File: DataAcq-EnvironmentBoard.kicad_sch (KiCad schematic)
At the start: 23 parts, among them J1 CAN Output, J2 CAN Input, U1 SHT45, U2 FS3000-1005, U3 LMT87DCK, U4 Daughterboard Connector

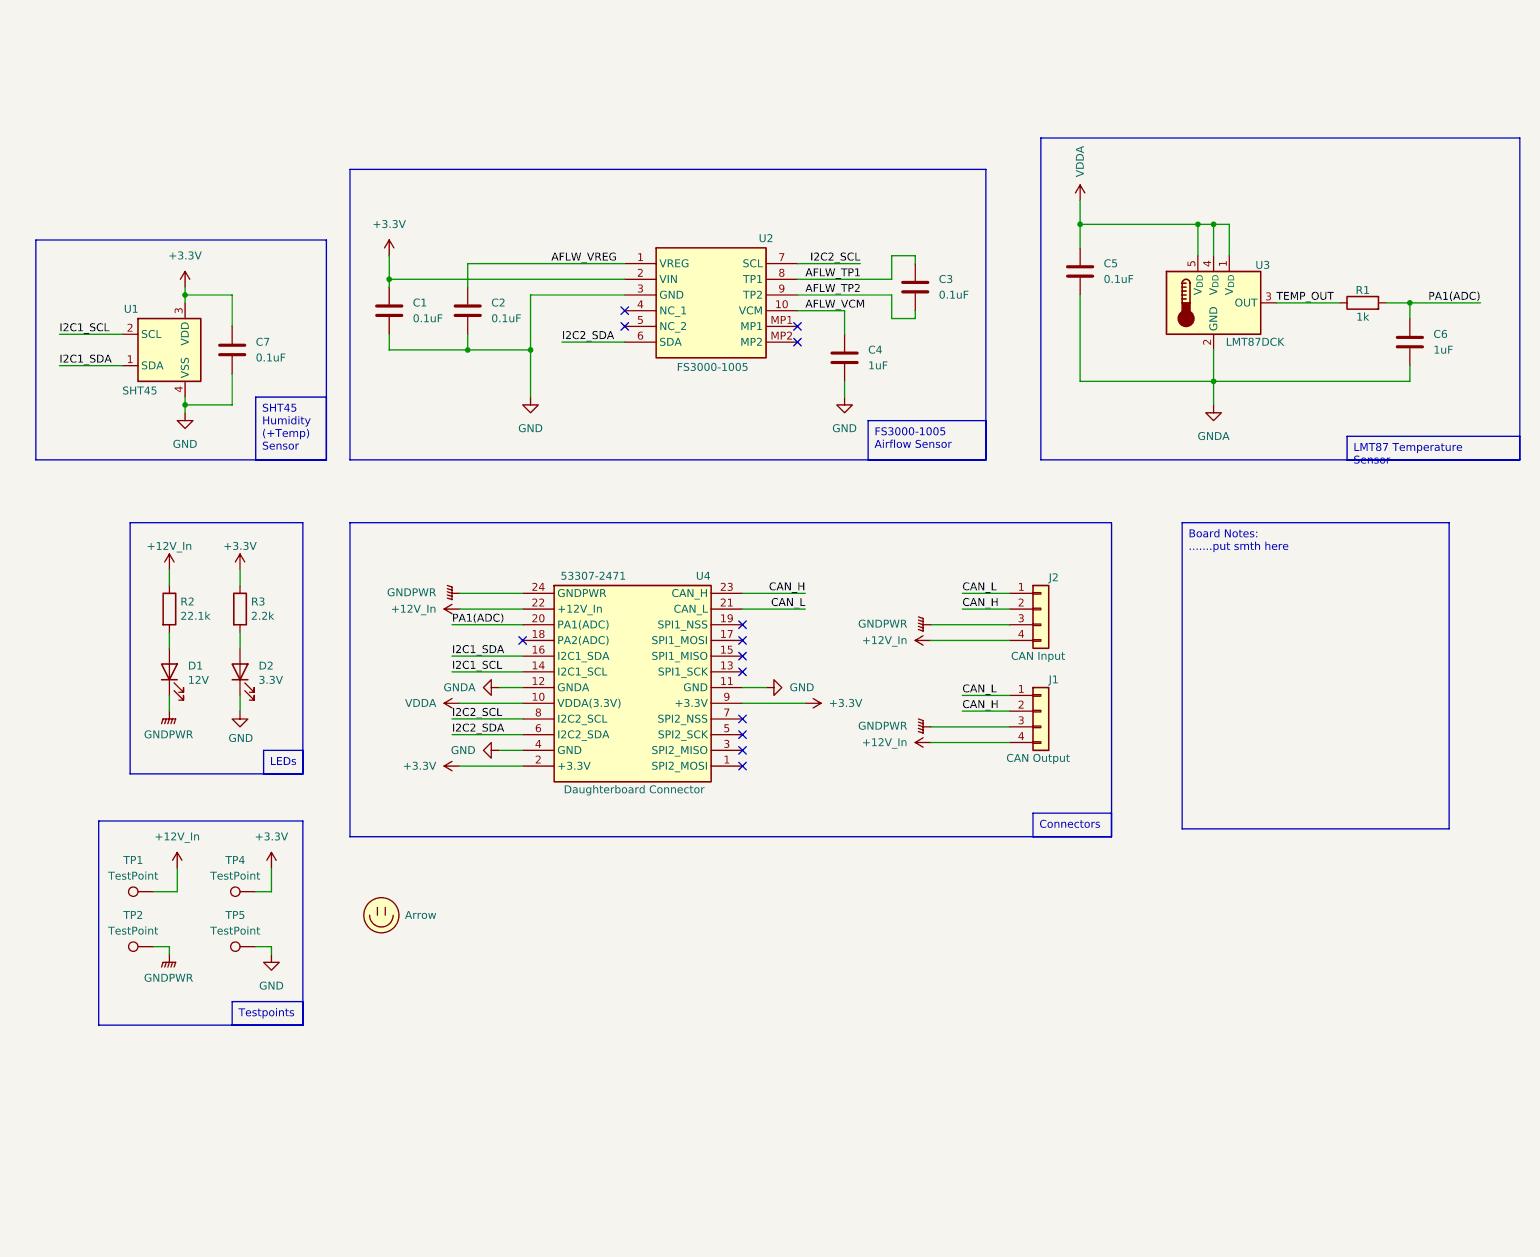
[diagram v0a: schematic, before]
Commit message: change sch to match new symbols
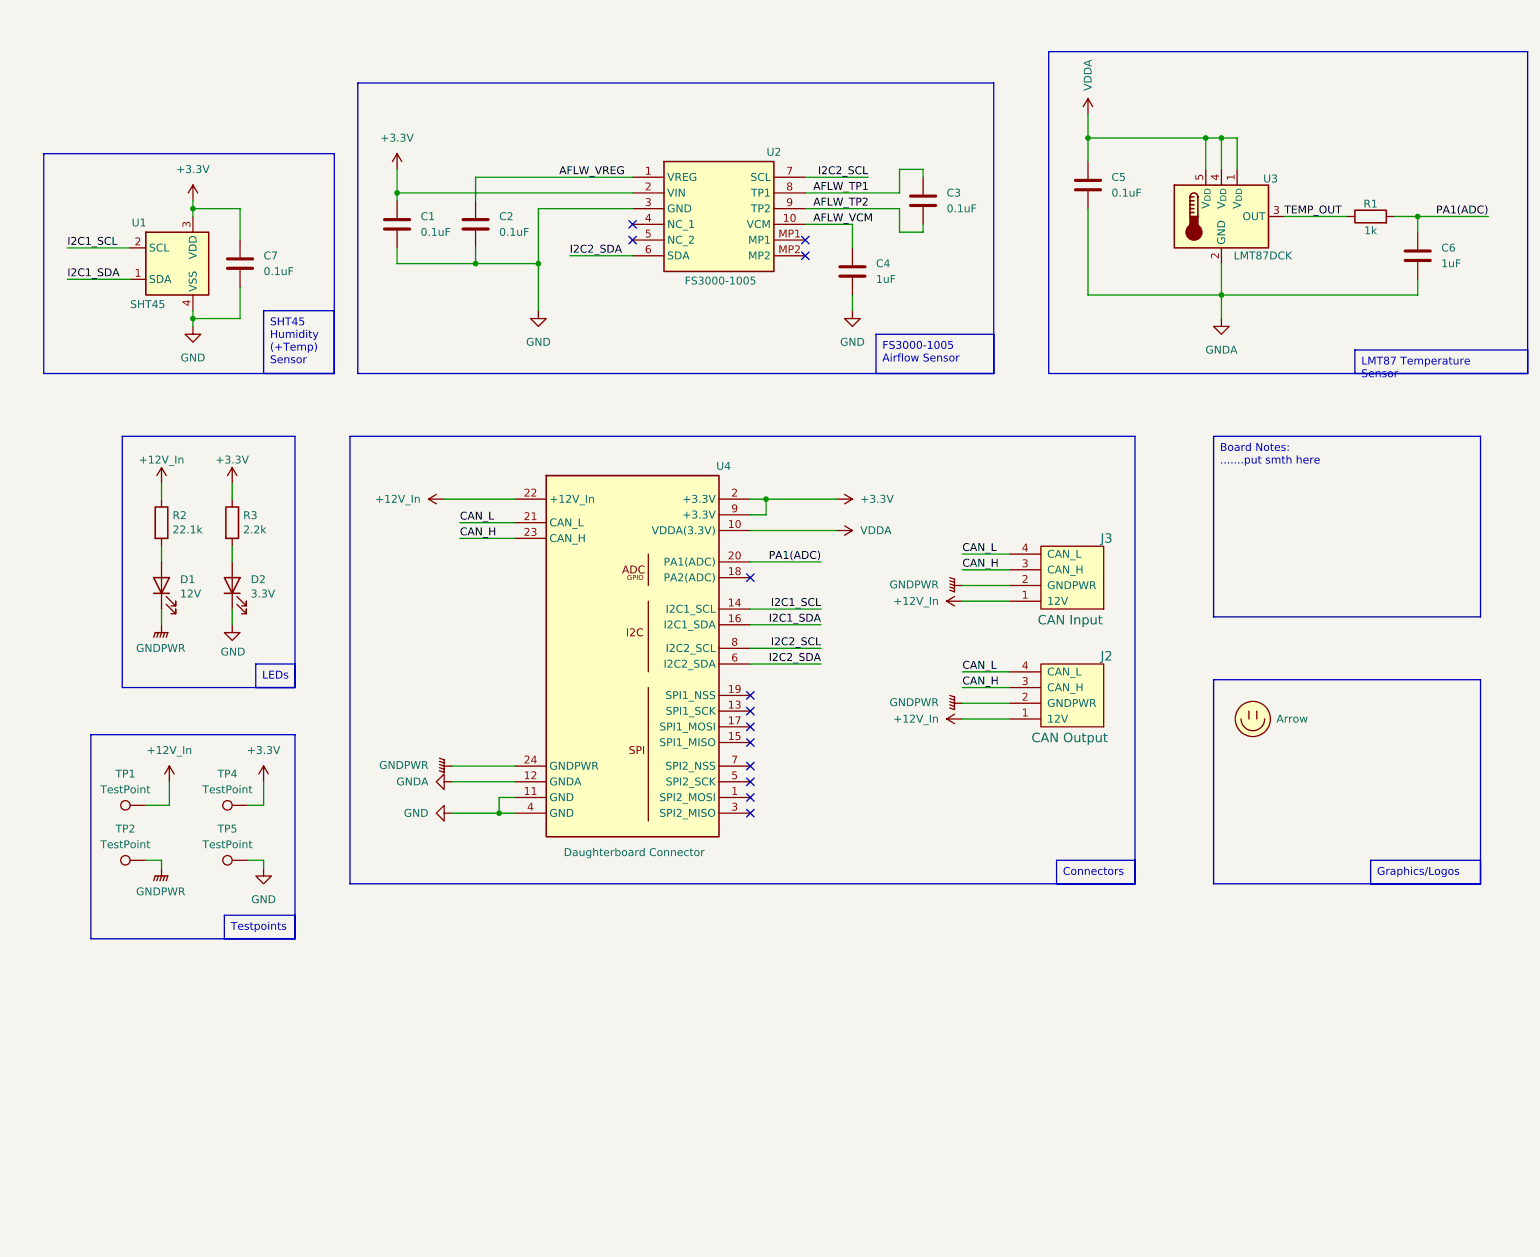
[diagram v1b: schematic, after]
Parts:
- removed J1: CAN Output, UTSVT_Connectors:Molex_MicroFit3.0_1x4xP3.00mm_PolarizingPeg_Vertical, symbol Connector_Generic:Conn_01x04
- removed J2: CAN Input, UTSVT_Connectors:Molex_MicroFit3.0_1x4xP3.00mm_PolarizingPeg_Vertical, symbol Connector_Generic:Conn_01x04
- added J2: CAN Output, UTSVT_Connectors:Molex_MicroFit3.0_1x4xP3.00mm_PolarizingPeg_Vertical, symbol utsvt-connectors:PeripheralCANConnector
- added J3: CAN Input, UTSVT_Connectors:Molex_MicroFit3.0_1x4xP3.00mm_PolarizingPeg_Vertical, symbol utsvt-connectors:PeripheralCANConnector
- U2: footprint SamacSys_Parts:FS30001005 -> FS30001005
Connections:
- net +12V_In: now also J2.1 (12V), J3.1 (12V)
- net CAN_H: now also J2.3 (CAN_H), J3.3 (CAN_H)
- net CAN_L: now also J2.4 (CAN_L), J3.4 (CAN_L)
- net GNDPWR: now also J2.2 (GNDPWR), J3.2 (GNDPWR)
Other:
- moved on the sheet: C1, C2, C3, C4, C5, C6, C7, D1, D2, R1, R2, R3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

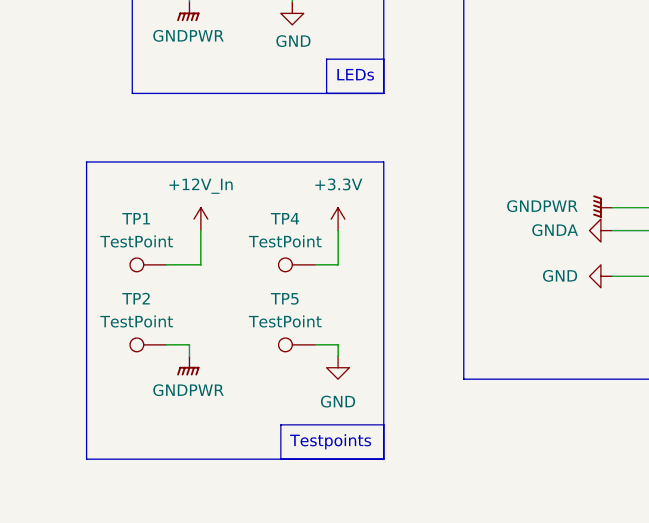
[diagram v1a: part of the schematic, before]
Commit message: add test point and redo CAN connections
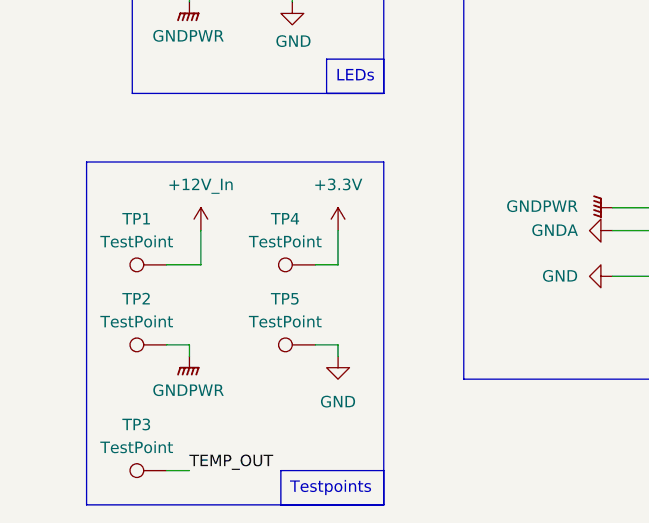
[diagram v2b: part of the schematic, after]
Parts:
- added TP3: TestPoint, UTSVT_Special:TestPoint_HEX_3mmID, symbol Connector:TestPoint
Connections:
- net TEMP_OUT: now also TP3.1
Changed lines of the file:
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@@
 	(wire
 		(pts
+			(xy 45.72 166.37) (xy 48.26 166.37)
+		)
+		(stroke
+			(width 0)
+			(type default)
+		)
+	)
+	(wire
+		(pts
 			(xy 160.02 60.96) (xy 160.02 63.5)
 		)
@@
 	(rectangle
 		(start 36.83 132.08)
-		(end 69.85 165.1)
+		(end 69.85 170.18)
 		(stroke
 			(width 0)
@@
 	(text_box "Testpoints"
 		(exclude_from_sim no)
-		(at 58.42 161.29 0)
+		(at 58.42 166.37 0)
 		(size 11.43 3.81)
 		(stroke
@@
 		)
 	)
+	(label "TEMP_OUT"
+		(at 48.26 166.37 0)
+		(fields_autoplaced yes)
+		(effects
+			(font
+				(size 1.27 1.27)
+			)
+			(justify left bottom)
+		)
+	)
 	(symbol
 		(lib_id "utsvt-connectors:PeripheralCANConnector")
@@
 					(unit 1)
 				)
+			)
+		)
+	)
+	(symbol
+		(lib_id "Connector:TestPoint")
+		(at 45.72 166.37 90)
+		(unit 1)
+		(exclude_from_sim no)
+		(in_bom yes)
+		(on_board yes)
+		(dnp no)
+		(fields_autoplaced yes)
+		(property "Reference" "TP3"
+			(at 42.418 161.29 90)
+			(effects
+				(font
+					(size 1.27 1.27)
+				)
+			)
+		)
+		(property "Value" "TestPoint"
+			(at 42.418 163.83 90)
+			(effects
+				(font
+					(size 1.27 1.27)
+				)
+			)
+		)
+		(property "Footprint" "UTSVT_Special:TestPoint_HEX_3mmID"
+			(at 45.72 161.29 0)
+			(effects
+				(font
+					(size 1.27 1.27)
+				)
+				(hide yes)
+			)
+		)
+		(property "Datasheet" "~"
+			(at 45.72 161.29 0)
+			(effects
+				(font
+					(size 1.27 1.27)
+				)
+				(hide yes)
+			)
+		)
+		(property "Description" "test point"
+			(at 45.72 166.37 0)
+			(effects
+				(font
+					(size 1.27 1.27)
+				)
+				(hide yes)
+			)
+		)
+		(property "PN" ""
+			(at 45.72 166.37 0)
+			(effects
+				(font
+					(size 1.27 1.27)
+				)
+				(hide yes)
+			)
+		)
+		(property "p/n" ""
+			(at 45.72 166.37 0)
+			(effects
+				(font
+					(size 1.27 1.27)
+				)
+				(hide yes)
+			)
+		)
+		(pin "1"
+		)
+		(instances
+			(project "DataAcq-EnvironmentBoard"
+				(path "/bc5fb1f8-c603-414b-89d1-18cc156ddb66"
+					(reference "TP3")
+					(unit 1)
+				)

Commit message: add images and cleanup
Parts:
- added LOGO2: Dr. Hallock, UTSVT_Special:Hallock_Image_Tiny, symbol utsvt-misc:Logo_Placeholder
- added LOGO3: UTSVT Logo, UTSVT_Special:UTSVT_Logo_Symbol, symbol utsvt-misc:Logo_Placeholder
- added LOGO4: Wolf, images:wolf, symbol utsvt-misc:Logo_Placeholder
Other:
- moved on the sheet: C5
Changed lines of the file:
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@@
 	(wire
 		(pts
-			(xy 198.12 35.56) (xy 198.12 39.37)
+			(xy 198.12 35.56) (xy 198.12 44.45)
 		)
 		(stroke
@@
 	(wire
 		(pts
-			(xy 198.12 46.99) (xy 198.12 60.96)
+			(xy 198.12 52.07) (xy 198.12 60.96)
 		)
 		(stroke
@@
 	)
 	(symbol
+		(lib_id "utsvt-misc:Logo_Placeholder")
+		(at 224.79 147.32 0)
+		(unit 1)
+		(exclude_from_sim no)
+		(in_bom yes)
+		(on_board yes)
+		(dnp no)
+		(fields_autoplaced yes)
+		(property "Reference" "LOGO3"
+			(at 224.79 143.51 0)
+			(effects
+				(font
+					(size 1.27 1.27)
+				)
+				(hide yes)
+			)
+		)
+		(property "Value" "UTSVT Logo"
+			(at 228.6 147.3199 0)
+			(effects
+				(font
+					(size 1.27 1.27)
+				)
+				(justify left)
+			)
+		)
+		(property "Footprint" "UTSVT_Special:UTSVT_Logo_Symbol"
+			(at 224.79 145.415 0)
+			(effects
+				(font
+					(size 1.27 1.27)
+				)
+				(hide yes)
+			)
+		)
+		(property "Datasheet" ""
+			(at 224.79 145.415 0)
+			(effects
+				(font
+					(size 1.27 1.27)
+				)
+				(hide yes)
+			)
+		)
+		(property "Description" "Graph footprint placeholder"
+			(at 224.79 147.32 0)
+			(effects
+				(font
+					(size 1.27 1.27)
+				)
+				(hide yes)
+			)
+		)
+		(instances
+			(project "DataAcq-EnvironmentBoard"
+				(path "/bc5fb1f8-c603-414b-89d1-18cc156ddb66"
+					(reference "LOGO3")
+					(unit 1)
+				)
+			)
+		)
+	)
+	(symbol
 		(lib_id "Device:C")
-		(at 198.12 43.18 0)
+		(at 198.12 48.26 0)
 		(unit 1)
 		(exclude_from_sim no)
@@
 		(fields_autoplaced yes)
 		(property "Reference" "C5"
-			(at 201.93 41.9099 0)
+			(at 201.93 46.9899 0)
 			(effects
 				(font
@@
 		)
 		(property "Value" "0.1uF"
-			(at 201.93 44.4499 0)
+			(at 201.93 49.5299 0)
 			(effects
 				(font
@@
 		)
 		(property "Footprint" "Capacitor_SMD:C_0805_2012Metric"
-			(at 199.0852 46.99 0)
+			(at 199.0852 52.07 0)
 			(effects
 				(font
@@
 		)
 		(property "Datasheet" "~"
-			(at 198.12 43.18 0)
+			(at 198.12 48.26 0)
 			(effects
 				(font
@@
 		)
 		(property "Description" "Unpolarized capacitor"
-			(at 198.12 43.18 0)
+			(at 198.12 48.26 0)
 			(effects
 				(font
@@
 		)
 		(property "P/N" "C0805C104M5RACTU"
-			(at 198.12 43.18 0)
+			(at 198.12 48.26 0)
 			(effects
 				(font
@@
 	)
 	(symbol
+		(lib_id "utsvt-misc:Logo_Placeholder")
+		(at 245.11 129.54 0)
+		(unit 1)
+		(exclude_from_sim no)
+		(in_bom yes)
+		(on_board yes)
+		(dnp no)
+		(fields_autoplaced yes)
+		(property "Reference" "LOGO4"
+			(at 245.11 125.73 0)
+			(effects
+				(font
+					(size 1.27 1.27)
+				)
+				(hide yes)
+			)
+		)
+		(property "Value" "Wolf"
+			(at 248.92 129.5399 0)
+			(effects
+				(font
+					(size 1.27 1.27)
+				)
+				(justify left)
+			)
+		)
+		(property "Footprint" "images:wolf"
+			(at 245.11 127.635 0)
+			(effects
+				(font
+					(size 1.27 1.27)
+				)
+				(hide yes)
+			)
+		)
+		(property "Datasheet" ""
+			(at 245.11 127.635 0)
+			(effects
+				(font
+					(size 1.27 1.27)
+				)
+				(hide yes)
+			)
+		)
+		(property "Description" "Graph footprint placeholder"
+			(at 245.11 129.54 0)
+			(effects
+				(font
+					(size 1.27 1.27)
+				)
+				(hide yes)
+			)
+		)
+		(instances
+			(project "DataAcq-EnvironmentBoard"
+				(path "/bc5fb1f8-c603-414b-89d1-18cc156ddb66"
+					(reference "LOGO4")
+					(unit 1)
+				)
+			)
+		)
+	)
+	(symbol
 		(lib_id "power:GND")
 		(at 53.34 66.04 0)
@@
 					(unit 1)
 				)
+			)
+		)
+	)
+	(symbol
+		(lib_id "utsvt-misc:Logo_Placeholder")
+		(at 224.79 138.43 0)
+		(unit 1)
+		(exclude_from_sim no)
+		(in_bom yes)
+		(on_board yes)
+		(dnp no)
+		(fields_autoplaced yes)
+		(property "Reference" "LOGO2"
+			(at 224.79 134.62 0)
+			(effects
+				(font
+					(size 1.27 1.27)
+				)
+				(hide yes)
+			)
+		)
+		(property "Value" "Dr. Hallock"
+			(at 228.6 138.4299 0)
+			(effects
+				(font
+					(size 1.27 1.27)
+				)
+				(justify left)
+			)
+		)
+		(property "Footprint" "UTSVT_Special:Hallock_Image_Tiny"
+			(at 224.79 136.525 0)
+			(effects
+				(font
+					(size 1.27 1.27)
+				)
+				(hide yes)
+			)
+		)
+		(property "Datasheet" ""
+			(at 224.79 136.525 0)
+			(effects
+				(font
+					(size 1.27 1.27)
+				)
+				(hide yes)
+			)
+		)
+		(property "Description" "Graph footprint placeholder"
+			(at 224.79 138.43 0)
+			(effects
+				(font
+					(size 1.27 1.27)
+				)
+				(hide yes)
+			)
+		)
+		(instances
+			(project "DataAcq-EnvironmentBoard"
+				(path "/bc5fb1f8-c603-414b-89d1-18cc156ddb66"
+					(reference "LOGO2")
+					(unit 1)
+				)

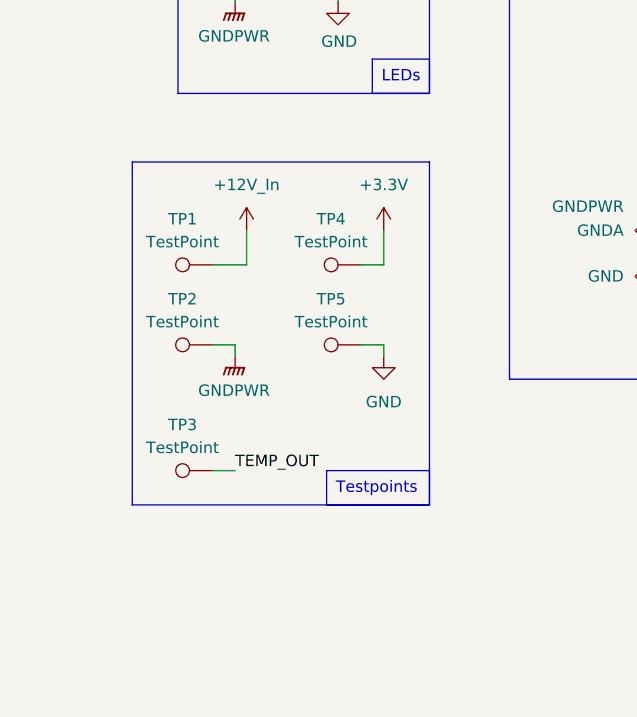
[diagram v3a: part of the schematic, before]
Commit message: add i2c testpoints to sch
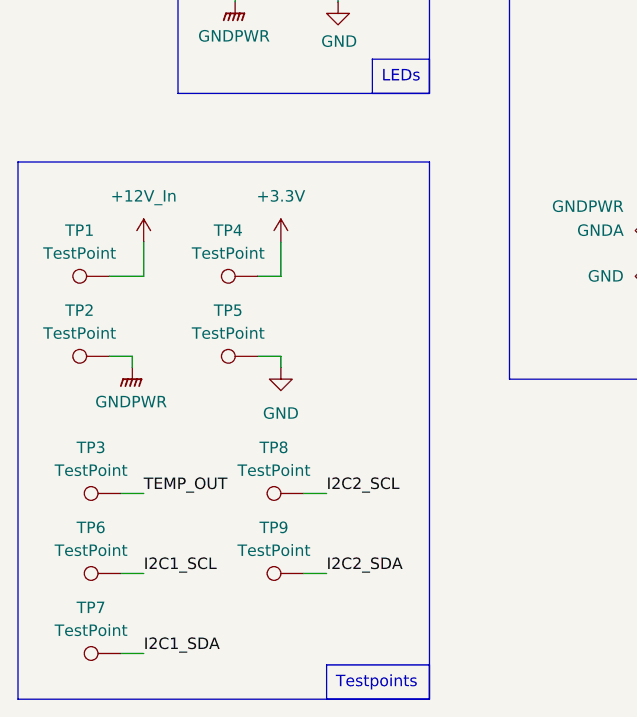
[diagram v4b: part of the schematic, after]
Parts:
- added TP6, TP7, TP8, TP9: TestPoint, UTSVT_Special:TestPoint_HEX_3mmID, symbol Connector:TestPoint
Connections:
- net I2C1_SCL: now also TP6.1
- net I2C1_SDA: now also TP7.1
- net I2C2_SCL: now also TP8.1
- net I2C2_SDA: now also TP9.1
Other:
- moved on the sheet: TP1, TP2, TP3, TP4, TP5

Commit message: move passives to sensor side, reroute temp sensor
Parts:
- TP6, TP7, TP8, TP9: footprint UTSVT_Special:TestPoint_HEX_3mmID -> Connector_PinHeader_2.54mm:PinHeader_1x01_P2.54mm_Vertical
- U2: footprint FS30001005 -> SamacSys_Parts:FS30001005
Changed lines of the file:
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@@
 			)
 		)
-		(property "Footprint" "UTSVT_Special:TestPoint_HEX_3mmID"
+		(property "Footprint" "Connector_PinHeader_2.54mm:PinHeader_1x01_P2.54mm_Vertical"
 			(at 35.56 172.72 0)
 			(effects
@@
 			)
 		)
-		(property "Footprint" "UTSVT_Special:TestPoint_HEX_3mmID"
+		(property "Footprint" "Connector_PinHeader_2.54mm:PinHeader_1x01_P2.54mm_Vertical"
 			(at 55.88 163.83 0)
 			(effects
@@
 			)
 		)
-		(property "Footprint" "UTSVT_Special:TestPoint_HEX_3mmID"
+		(property "Footprint" "Connector_PinHeader_2.54mm:PinHeader_1x01_P2.54mm_Vertical"
 			(at 35.56 181.61 0)
 			(effects
@@
 			)
 		)
-		(property "Footprint" "UTSVT_Special:TestPoint_HEX_3mmID"
+		(property "Footprint" "Connector_PinHeader_2.54mm:PinHeader_1x01_P2.54mm_Vertical"
 			(at 55.88 172.72 0)
 			(effects
@@
 			)
 		)
-		(property "Footprint" "FS30001005"
+		(property "Footprint" "SamacSys_Parts:FS30001005"
 			(at 148.59 136.83 0)
 			(effects
